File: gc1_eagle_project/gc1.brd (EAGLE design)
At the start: 47.9 x 83.8 mm, 9 parts

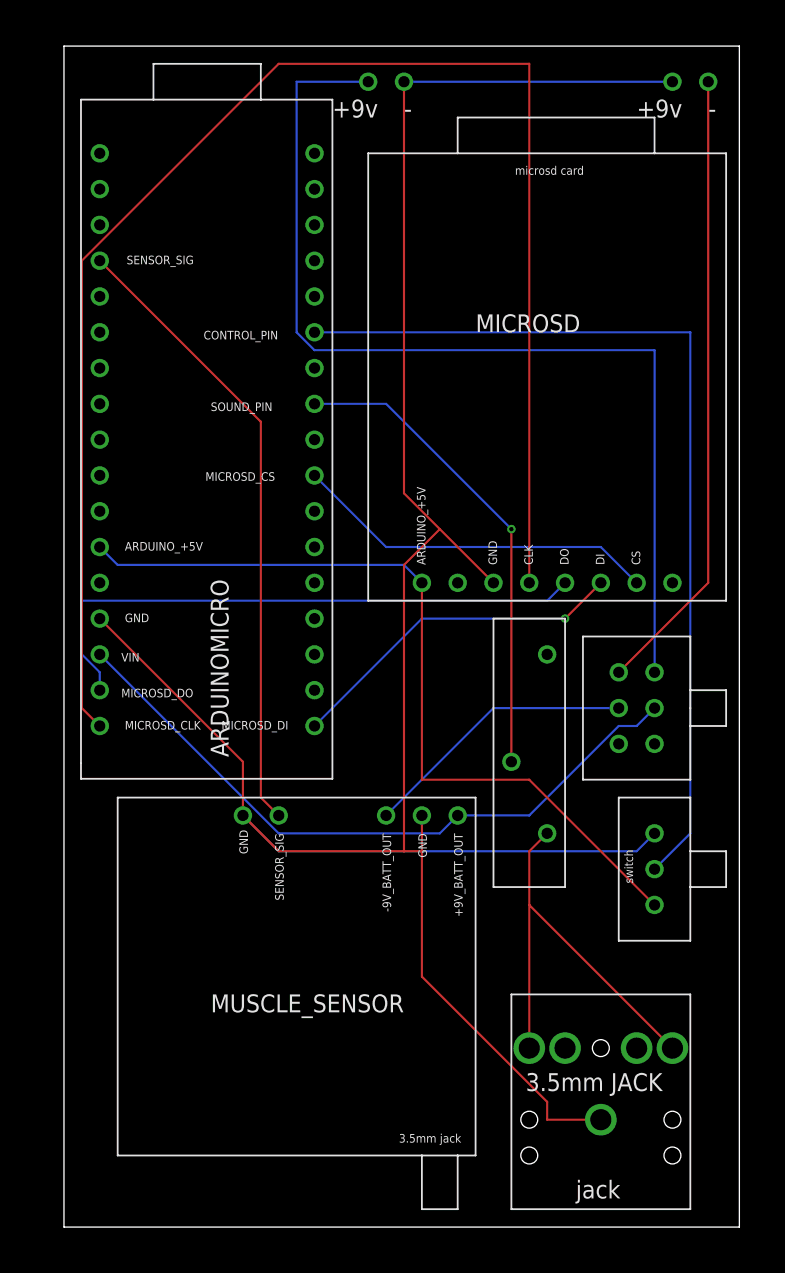
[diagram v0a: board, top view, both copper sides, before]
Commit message: swapped some parts, added 10k resistor between arduino 5v and control pin
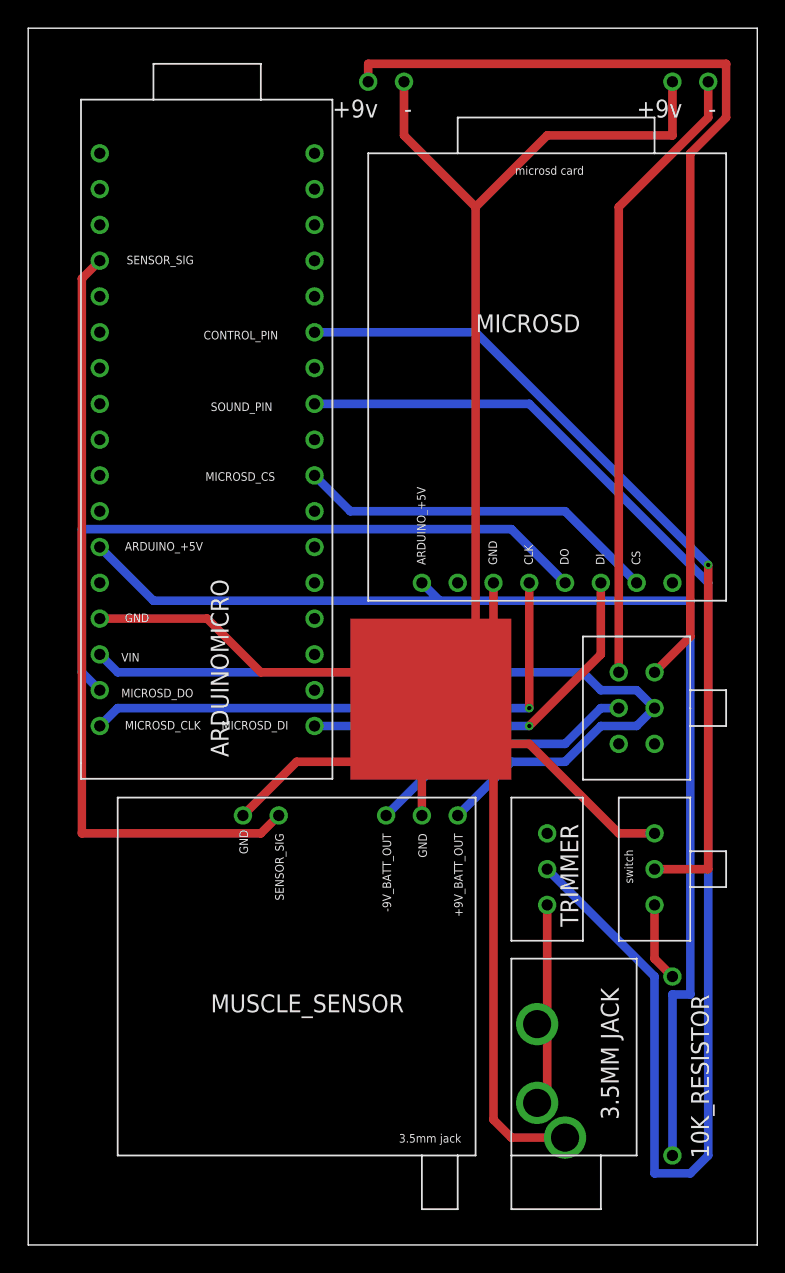
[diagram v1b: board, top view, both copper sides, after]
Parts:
- removed U$7: TRIMPOT_3006, gc1_parts:TRIMPOT_3006
- removed U$8: STEREOJACK_35RAPC2BHN2, gc1_parts:STEREOJACK_35RAPC2BHN2
- added 10K_RESISTOR: 10K_RESISTOR, gc1_parts:10K_RESISTOR
- added 3.5MMJACK: 35RAPC2BVN4, gc1_parts:35RAPC4BVN4
- added TRIMMER: 66WR1KLF, gc1_parts:66WR1KLF
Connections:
- new net +5V_RESISTOR: 10K_RESISTOR.2, U$9.3
- net ARDUINO_+5V: now also 10K_RESISTOR.1; no longer U$9.3
- net AUDIO_SIGNAL: now also 3.5MMJACK.2, 3.5MMJACK.4, TRIMMER.3; no longer U$7.3, U$8.LEFT, U$8.RIGHT
- net GND: now also 3.5MMJACK.1; no longer U$8.GROUND
- net SOUND_PIN: now also TRIMMER.2; no longer U$7.2
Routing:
- net SOUND_PIN: track 34.2 -> 102.9 mm, vias 1 -> 0
- net MICROSD_CLK: track 107.9 -> 39.9 mm, vias 0 -> 1
- net ARDUINO_+5V: track 58.1 -> 85.9 mm
- net AUDIO_SIGNAL: track 30.1 -> 15.3 mm
- net SENSOR_SIG: track 44.6 -> 55.7 mm
- net +9V_BATT_OUT: track 48.3 -> 58.1 mm
- net MICROSD_DO: track 41.7 -> 47.8 mm
- net CONTROL_PIN: track 65.8 -> 60.2 mm, vias 0 -> 1
- net +5V_RESISTOR: track 0.00 -> 5.61 mm
- net MICROSD_DI: track 24.5 -> 27.5 mm
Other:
- board size 47.9 x 83.8 mm -> 51.7 x 86.4 mm

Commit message: added copper fill
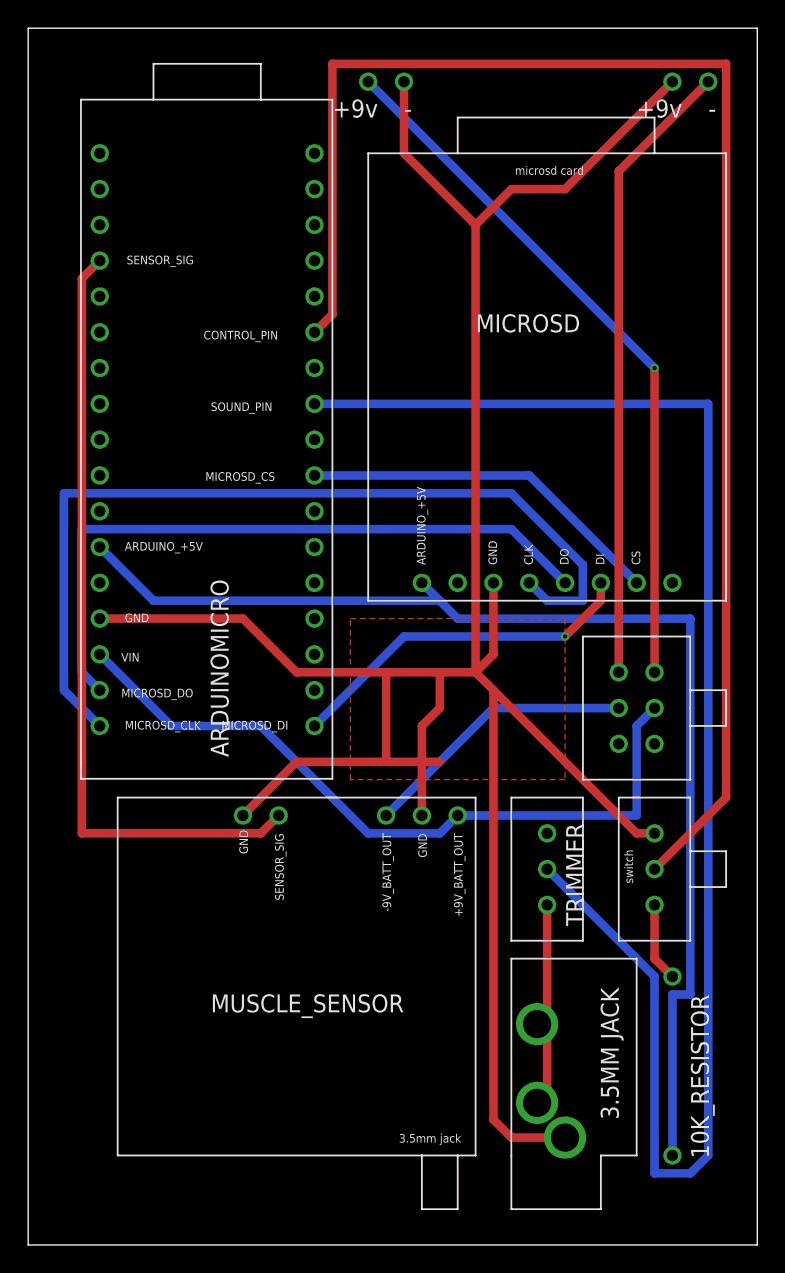
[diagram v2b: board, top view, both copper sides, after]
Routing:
- net CONTROL_PIN: track 60.2 -> 106.8 mm, vias 1 -> 0
- net MICROSD_CLK: track 39.9 -> 63.4 mm, vias 1 -> 0
- net +9V_BATT_IN: track 72.0 -> 50.3 mm, vias 0 -> 1
- net GND: track 172.6 -> 183.4 mm
- net SOUND_PIN: track 102.9 -> 110.4 mm
- net +9V_BATT_OUT: track 58.1 -> 52.0 mm
- net MICROSD_DI: track 27.5 -> 25.3 mm
- net ARDUINO_+5V: track 85.9 -> 85.2 mm
- added copper zone on layer 1, net GND
